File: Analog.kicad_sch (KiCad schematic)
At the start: 6 parts

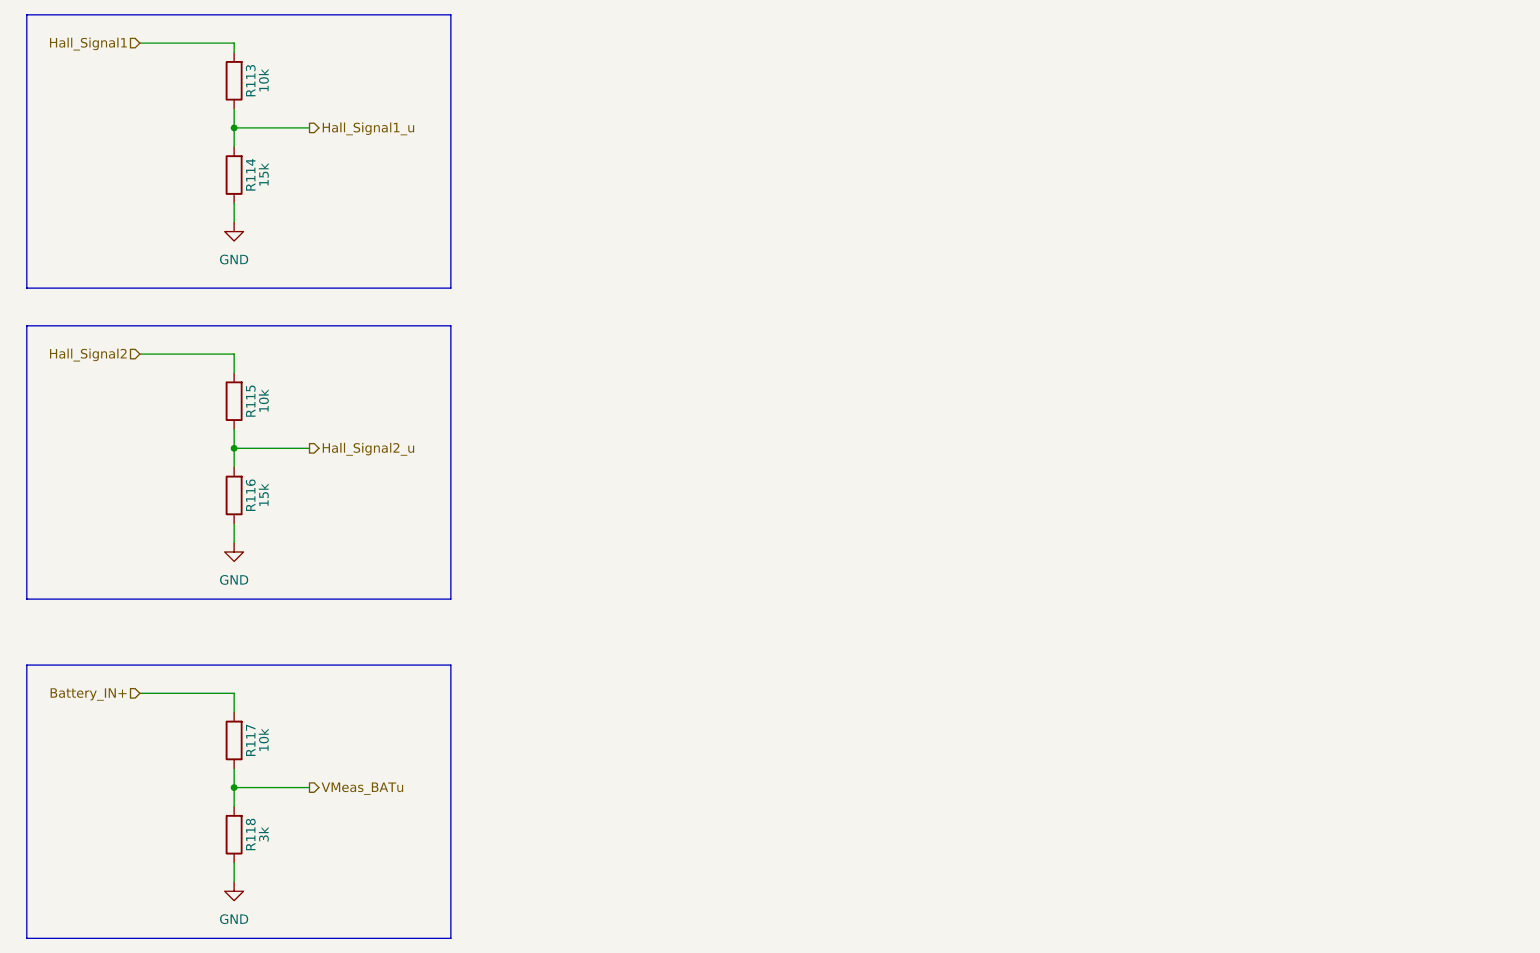
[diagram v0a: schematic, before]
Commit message: Added gyro, current sense, removed servo control, added temp sense
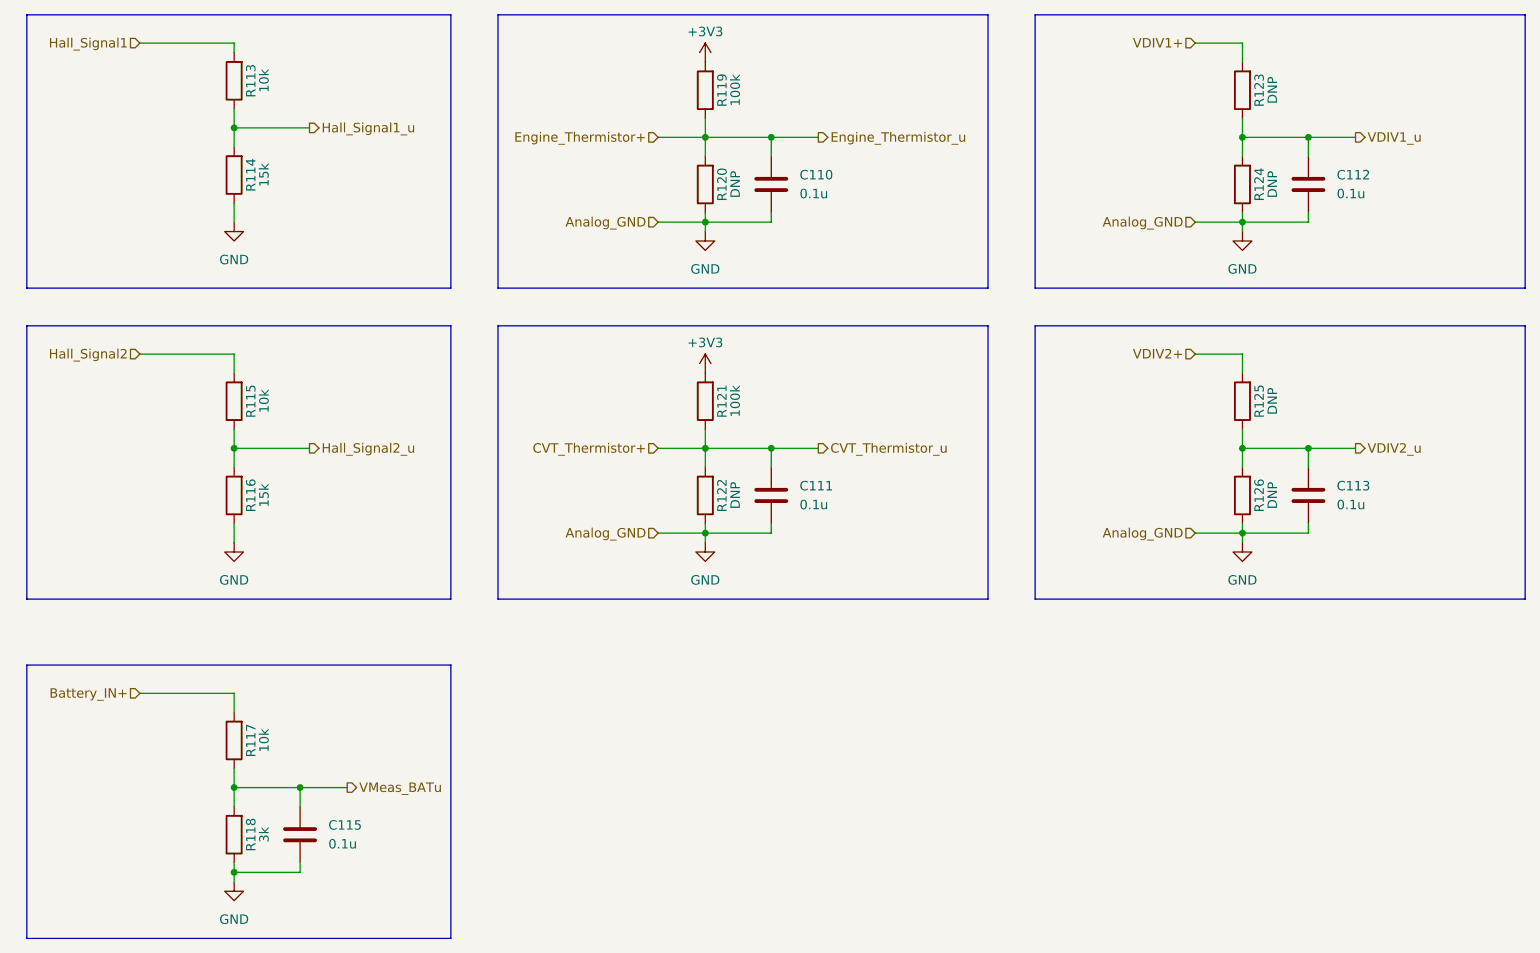
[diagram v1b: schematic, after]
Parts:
- added C110, C111, C112, C113, C115: 0.1u, Capacitor_SMD:C_0805_2012Metric_Pad1.18x1.45mm_HandSolder, symbol Device:C
- added R119, R121: 100k, Resistor_SMD:R_0603_1608Metric_Pad0.98x0.95mm_HandSolder, symbol Device:R
- added R120, R122, R123, R124, R125, R126: DNP, Resistor_SMD:R_0603_1608Metric_Pad0.98x0.95mm_HandSolder, symbol Device:R
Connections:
- net GND: now also C110.2, C111.2, C112.2, C113.2, C115.2, R120.1, R122.1, R124.1, R126.1
- net VMeas_BATu: now also C115.1
- new net +3V3: R119.2, R121.2
- new net CVT_Thermistor+: C111.1, R121.1, R122.2
- new net Engine_Thermistor+: C110.1, R119.1, R120.2
- new net VDIV1+: R123.2
- new net VDIV1_u: C112.1, R123.1, R124.2
- new net VDIV2+: R125.2
- new net VDIV2_u: C113.1, R125.1, R126.2

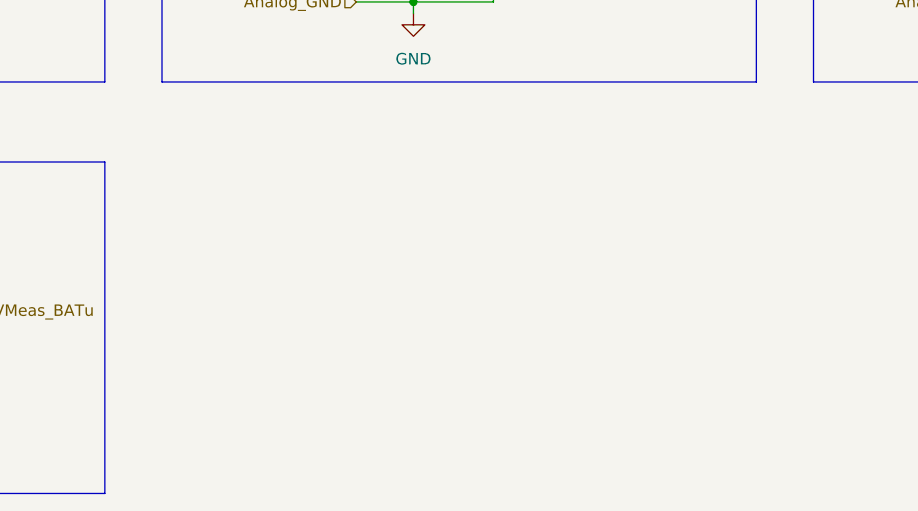
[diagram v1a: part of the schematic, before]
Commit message: finished up schematic, added magnetic sensor, cleaned up pins, etc.
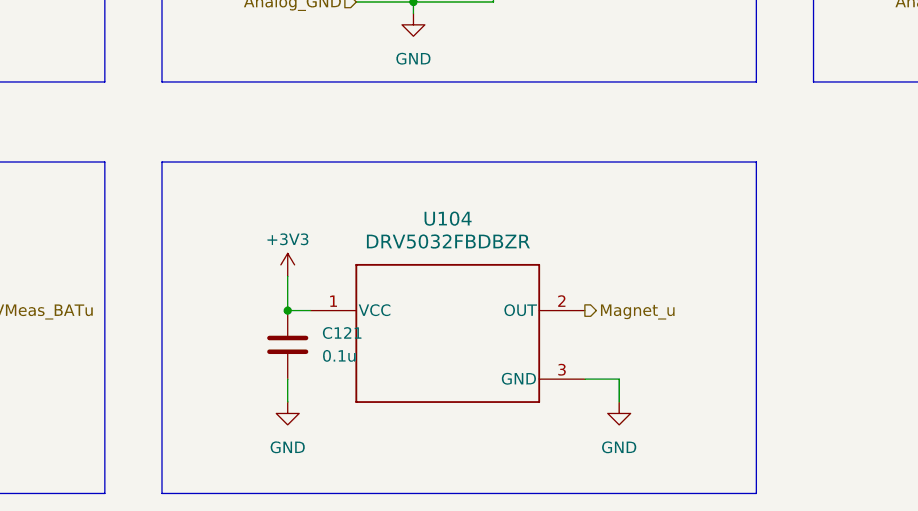
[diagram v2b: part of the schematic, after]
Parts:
- added C121: 0.1u, Capacitor_SMD:C_0603_1608Metric_Pad1.08x0.95mm_HandSolder, symbol Device:C
- added U104: DRV5032FBDBZR, DRV5032:DBZ0003A-IPC_A, symbol DRV5032:DRV5032FBDBZR
- C110, C111, C112, C113, C115: footprint Capacitor_SMD:C_0805_2012Metric_Pad1.18x1.45mm_HandSolder -> Capacitor_SMD:C_0603_1608Metric_Pad1.08x0.95mm_HandSolder; Digikey https://www.digikey.com/en/products/detail/murata-electroni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 -> (none)
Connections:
- net +3V3: now also C121.1, U104.1 (VCC)
- net GND: now also C121.2, U104.3 (GND)
- new net Magnet_u: U104.2 (OUT)

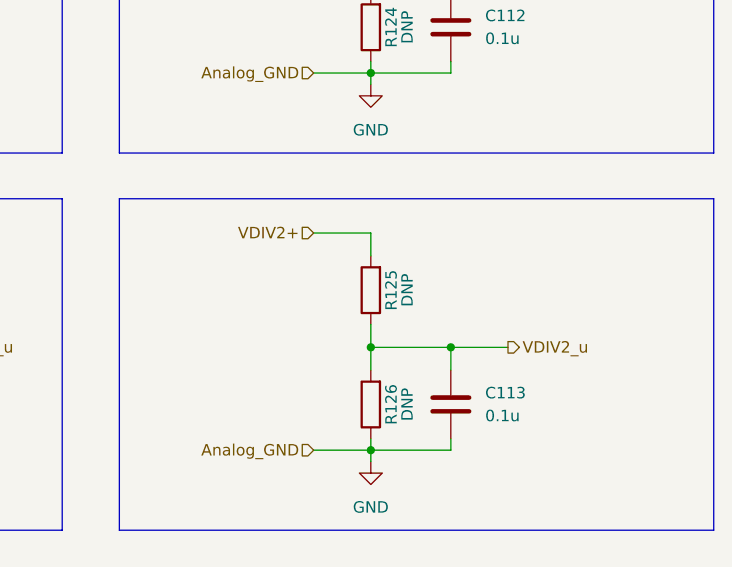
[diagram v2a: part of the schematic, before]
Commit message: removed a VDIV input and changed it to a thermistor input. Re-ran fabrication output
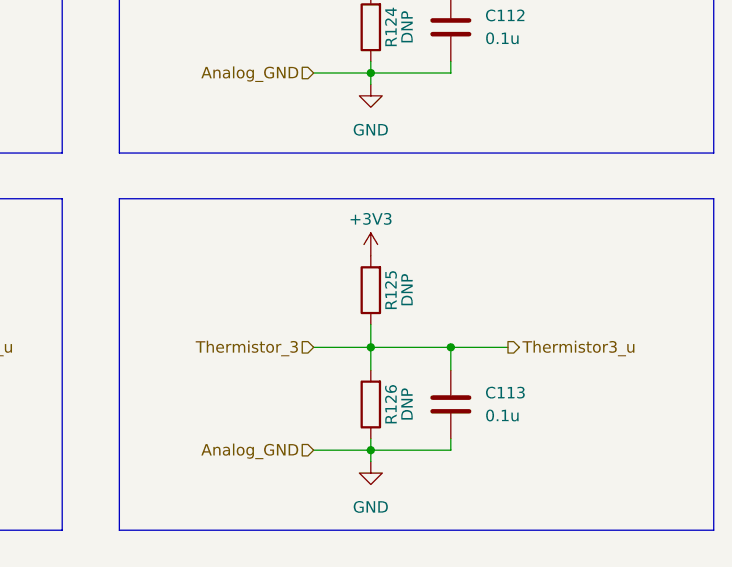
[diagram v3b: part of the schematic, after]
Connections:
- net VDIV2+ is gone; now on net +3V3: R125.2
- net VDIV2_u renamed Thermistor3_u
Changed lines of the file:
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@@
-	(wire
-		(pts
-			(xy 172.72 86.36) (xy 179.07 86.36)
-		)
-		(stroke
-			(width 0)
-			(type default)
-		)
-	)
 	(wire
 		(pts
@@
 	(wire
 		(pts
-			(xy 179.07 86.36) (xy 179.07 88.9)
-		)
-		(stroke
-			(width 0)
-			(type default)
-		)
-	)
-	(wire
-		(pts
 			(xy 30.48 86.36) (xy 43.18 86.36)
 		)
@@
 		(pts
 			(xy 179.07 96.52) (xy 179.07 99.06)
+		)
+		(stroke
+			(width 0)
+			(type default)
+		)
+	)
+	(wire
+		(pts
+			(xy 172.72 99.06) (xy 179.07 99.06)
 		)
 		(stroke
@@
 		)
 	)
+	(hierarchical_label "Thermistor_3"
+		(shape input)
+		(at 172.72 99.06 180)
+		(effects
+			(font
+				(size 1.27 1.27)
+			)
+			(justify right)
+		)
+	)
 	(hierarchical_label "Hall_Signal1"
 		(shape input)
@@
 		)
 	)
-	(hierarchical_label "VDIV2_u"
+	(hierarchical_label "Thermistor3_u"
 		(shape output)
 		(at 194.31 99.06 0)
@@
 		)
 	)
-	(hierarchical_label "VDIV2+"
-		(shape input)
-		(at 172.72 86.36 180)
-		(effects
-			(font
-				(size 1.27 1.27)
-			)
-			(justify right)
-		)
-	)
 	(hierarchical_label "Hall_Signal2"
 		(shape input)
@@
 					(unit 1)
 				)
+			)
+		)
+	)
+	(symbol
+		(lib_id "power:+3V3")
+		(at 179.07 88.9 0)
+		(unit 1)
+		(exclude_from_sim no)
+		(in_bom yes)
+		(on_board yes)
+		(dnp no)
+		(property "Reference" "#PWR0159"
+			(at 179.07 92.71 0)
+			(effects
+				(font
+					(size 1.27 1.27)
+				)
+				(hide yes)
+			)
+		)
+		(property "Value" "+3V3"
+			(at 179.07 84.836 0)
+			(effects
+				(font
+					(size 1.27 1.27)
+				)
+			)
+		)
+		(property "Footprint" ""
+			(at 179.07 88.9 0)
+			(effects
+				(font
+					(size 1.27 1.27)
+				)
+				(hide yes)
+			)
+		)
+		(property "Datasheet" ""
+			(at 179.07 88.9 0)
+			(effects
+				(font
+					(size 1.27 1.27)
+				)
+				(hide yes)
+			)
+		)
+		(property "Description" "Power symbol creates a global label with name \"+3V3\""
+			(at 179.07 88.9 0)
+			(effects
+				(font
+					(size 1.27 1.27)
+				)
+				(hide yes)
+			)
+		)
+		(pin "1"
+		)
+		(instances
+			(project "TeensyDAQ_REV0"
+				(path "/11737956-c422-45b5-a9a0-ee63a853502c/c3da58cd-cab8-4f7e-a189-a7bcb64c8919"
+					(reference "#PWR0159")
+					(unit 1)
+				)

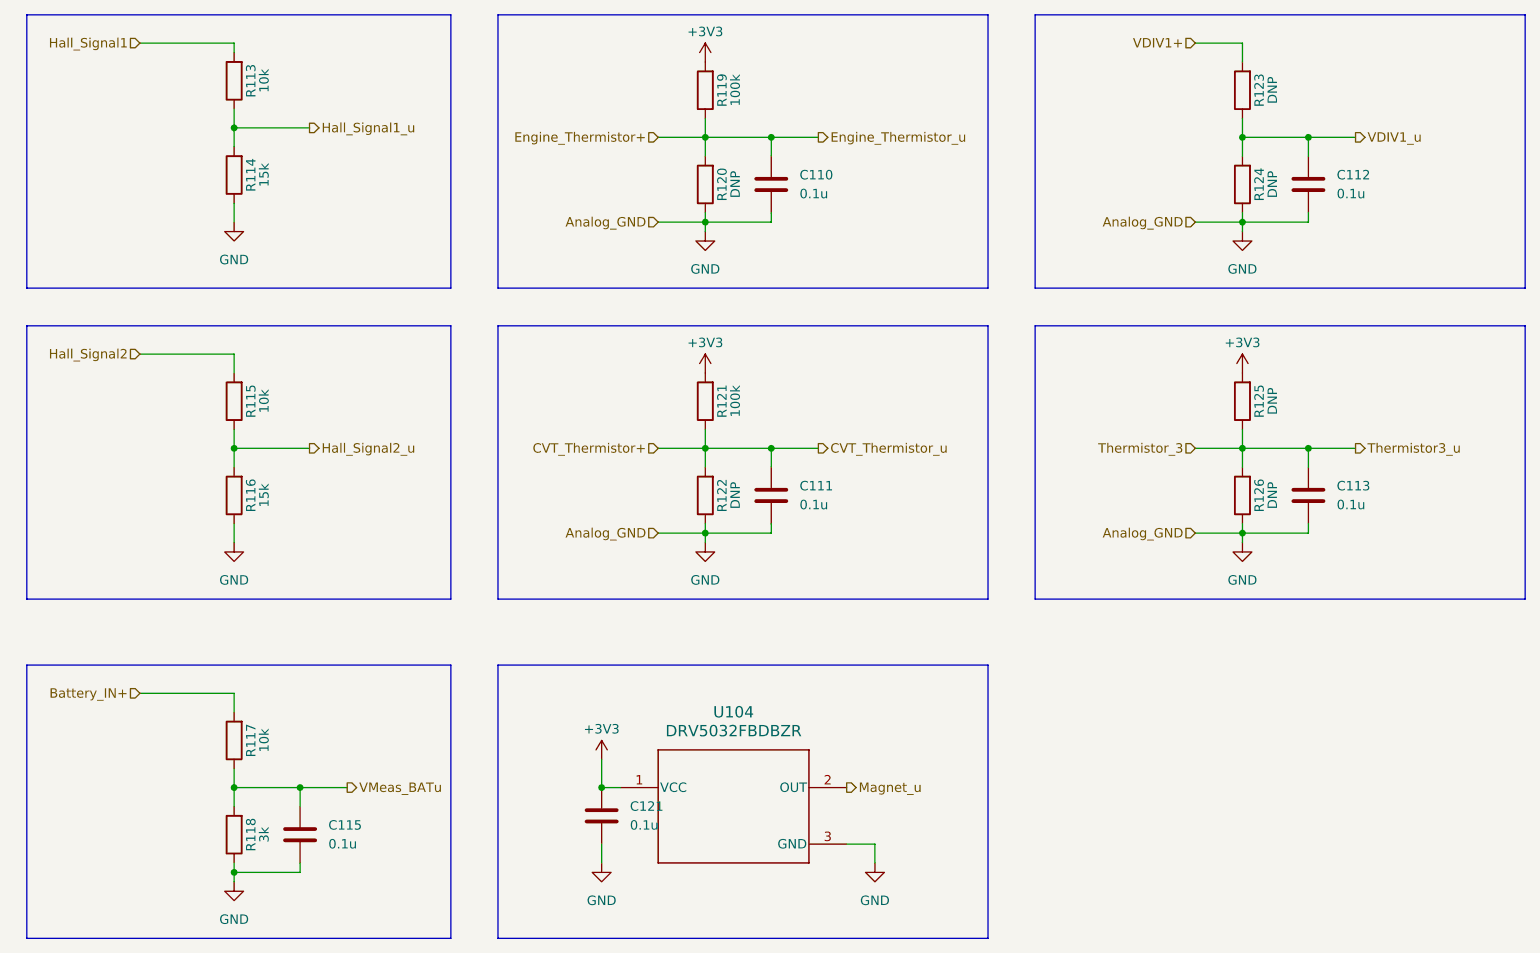
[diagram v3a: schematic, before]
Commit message: added TVS diodes to external pins for protection. Ran fabrication output. Ran iBOM generation. All part links can be seen in the iBOM. Download and open to see this
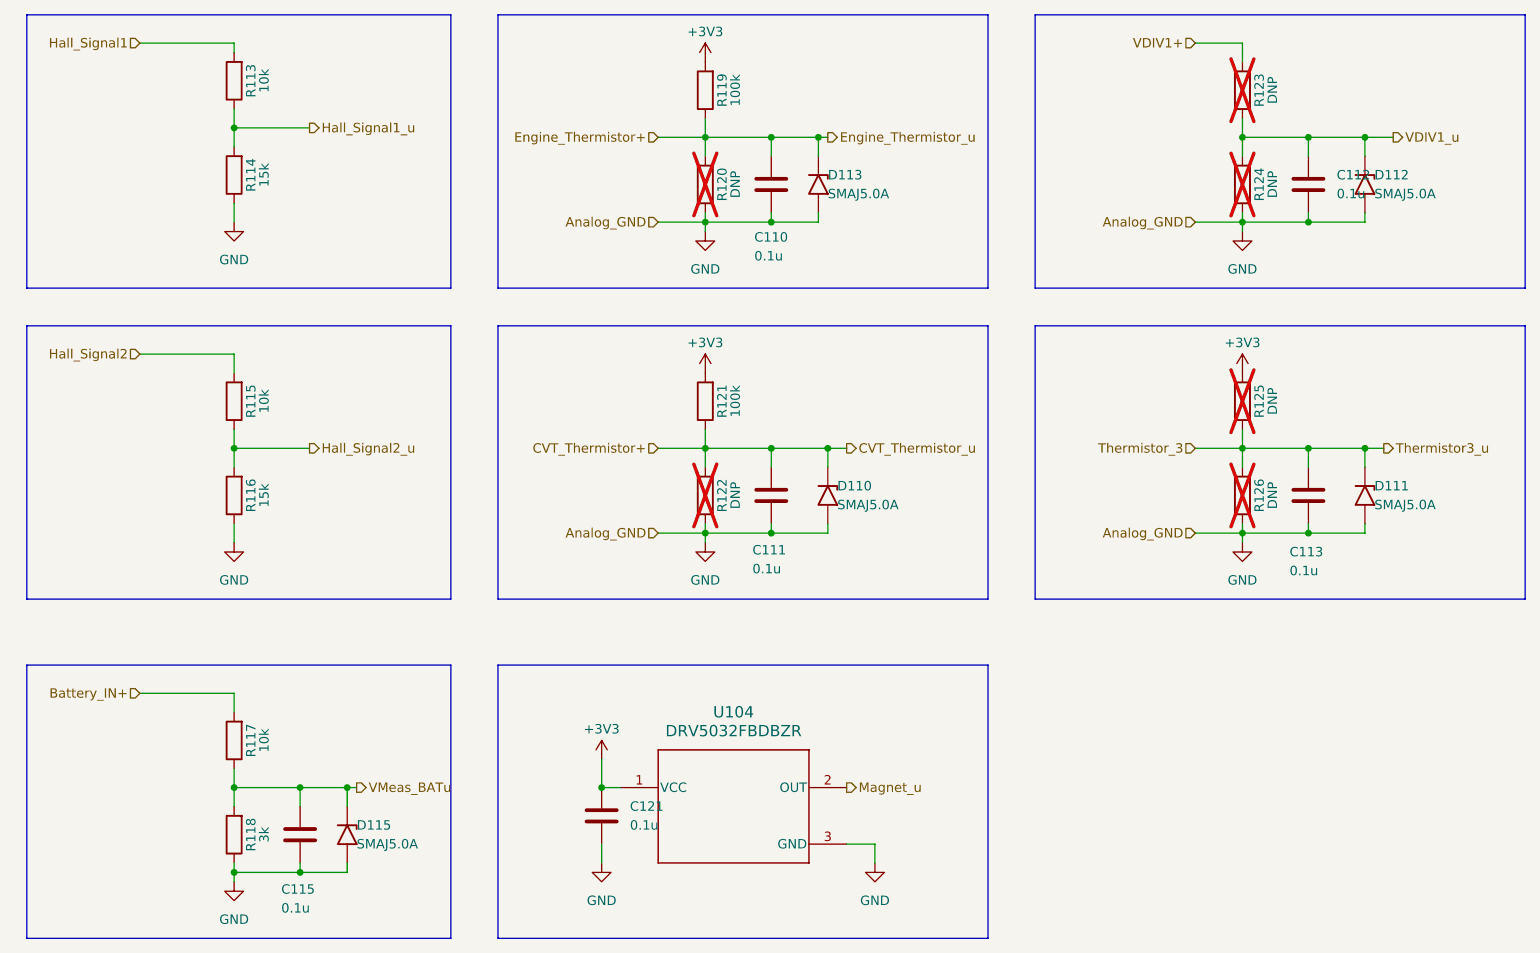
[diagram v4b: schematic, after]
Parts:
- added D110, D111, D112, D113, D115: SMAJ5.0A, Diode_SMD:D_SMA, symbol Diode:SMAJ5.0A
- C110, C111, C112, C113, C115, C121: DIGIKEY LINK (none) -> https://www.digikey.com/en/products/detail/murata-electroni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
- R113, R114, R115, R116, R117, R118, R119, R121: DIGIKEY LINK (none) -> https://www.digikey.com/en/products/detail/yageo/RC0603FR-0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
- R120, R122, R123, R124, R125, R126: now not fitted
- U104: DIGIKEY LINK (none) -> https://www.digikey.com/en/products/detail/texas-instrument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
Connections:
- net CVT_Thermistor+: now also D110.1 (A1)
- net Engine_Thermistor+: now also D113.1 (A1)
- net GND: now also D110.2 (A2), D111.2 (A2), D112.2 (A2), D113.2 (A2), D115.2 (A2)
- net Thermistor3_u: now also D111.1 (A1)
- net VDIV1_u: now also D112.1 (A1)
- net VMeas_BATu: now also D115.1 (A1)
